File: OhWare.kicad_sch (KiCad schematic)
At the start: 1 part, among them J1 Screw_Terminal_01x03

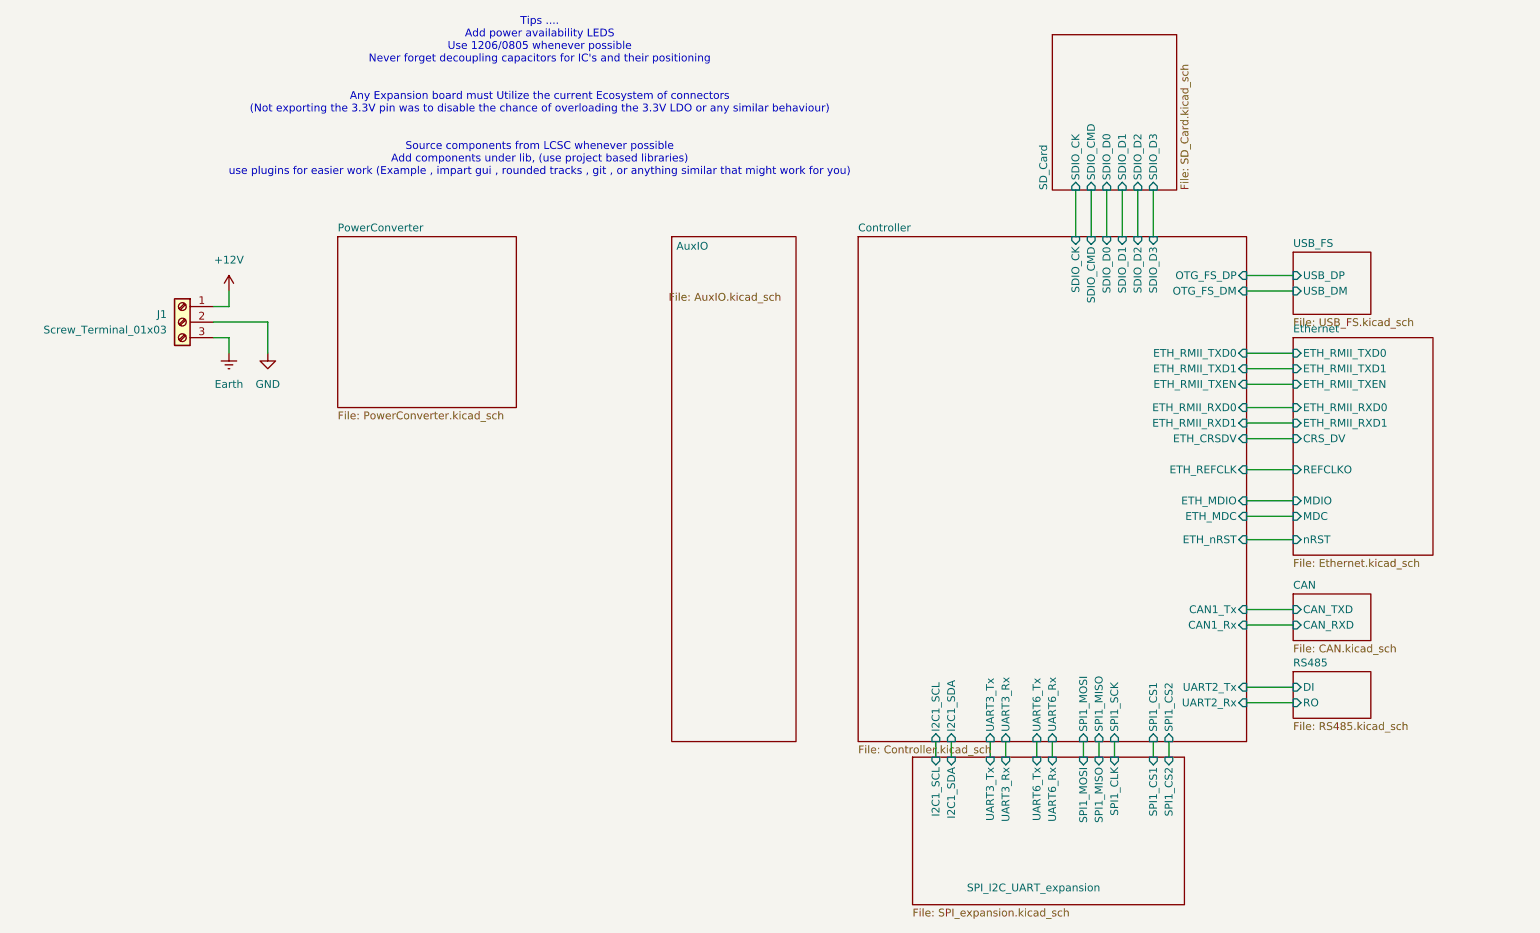
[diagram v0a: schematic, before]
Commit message: Done routing for Buck Converter , Rs485 and CAN , Some Routing for MCU and associated circuitry , NO ETHERNET ROUTING , NO module Interconnects yet
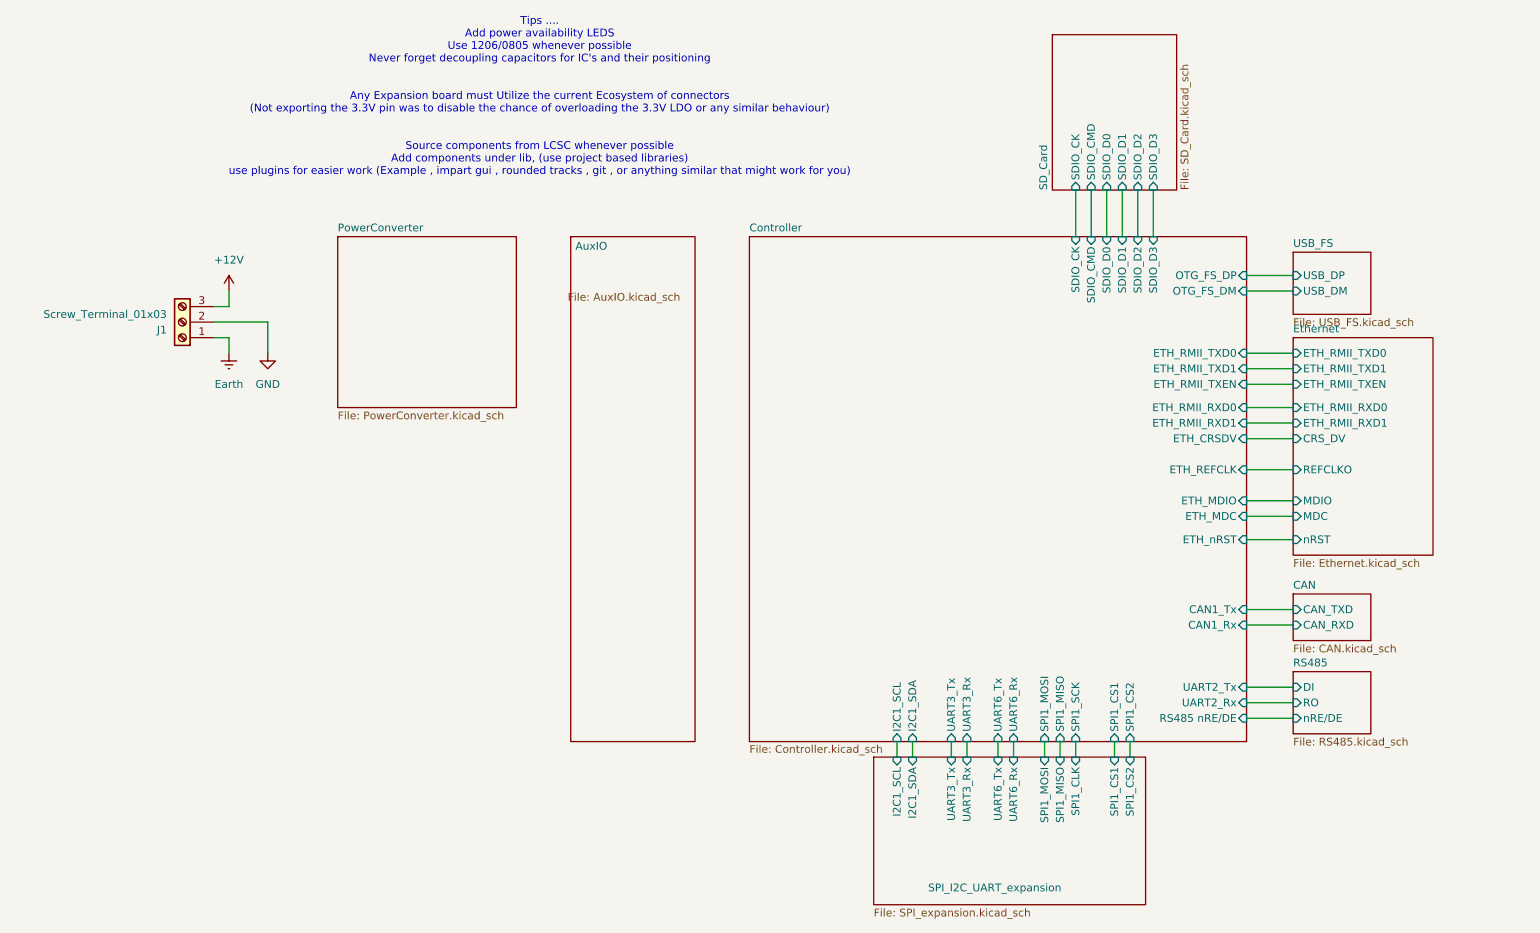
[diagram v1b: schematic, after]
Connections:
- net +12V: now also J1.3 (Pin_3); no longer J1.1 (Pin_1)
- net Earth: now also J1.1 (Pin_1); no longer J1.3 (Pin_3)
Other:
- sheet Controller ports: added RS485 nRE/DE; removed none
- sheet RS485 ports: added nRE/DE; removed none
- moved on the sheet: J1

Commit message: Added Base
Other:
- removed sheet Ethernet
- removed sheet SD_Card
- removed sheet USB_FS
- added sheet Esp32 (Esp32.kicad_sch)
- sheet Controller ports: added none; removed ETH_CRSDV, ETH_MDC, ETH_MDIO, ETH_REFCLK, ETH_RMII_RXD0, ETH_RMII_RXD1, ETH_RMII_TXD0, ETH_RMII_TXD1, ETH_RMII_TXEN, ETH_nRST, OTG_FS_DM, OTG_FS_DP, SDIO_CK, SDIO_CMD, SDIO_D0, SDIO_D1, SDIO_D2, SDIO_D3

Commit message: UPDATED
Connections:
- net +12V: now also J1.1 (Pin_1); no longer J1.3 (Pin_3)
- net Earth: now also J1.3 (Pin_3); no longer J1.1 (Pin_1)
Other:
- sheet Esp32 ports: added EN, SPI_CLK, SPI_CS, SPI_MISO, SPI_MOSI; removed none
- moved on the sheet: J1
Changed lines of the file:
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@@
 	(symbol
 		(lib_id "Connector:Screw_Terminal_01x03")
-		(at 40.64 69.85 180)
+		(at 40.64 69.85 0)
+		(mirror y)
 		(unit 1)
 		(exclude_from_sim no)
@@
 		(dnp no)
 		(property "Reference" "J1"
-			(at 38.1 71.1201 0)
+			(at 38.1 68.5799 0)
 			(effects
 				(font
@@
 		)
 		(property "Value" "Screw_Terminal_01x03"
-			(at 38.1 68.5801 0)
+			(at 38.1 71.1199 0)
 			(effects
 				(font
@@
 	)
 	(sheet
-		(at 222.25 72.39)
-		(size 19.05 21.59)
+		(at 222.25 73.66)
+		(size 19.05 17.78)
 		(exclude_from_sim no)
 		(in_bom yes)
@@
 		)
 		(property "Sheetname" "Esp32"
-			(at 222.25 71.6784 0)
+			(at 222.25 72.9484 0)
 			(effects
 				(font
@@
 		)
 		(property "Sheetfile" "Esp32.kicad_sch"
-			(at 222.25 94.5646 0)
+			(at 222.25 92.0246 0)
 			(effects
 				(font
@@
 			)
 		)
+		(pin "EN" input
+			(at 222.25 77.47 180)
+			(effects
+				(font
+					(size 1.27 1.27)
+				)
+				(justify left)
+			)
+		)
+		(pin "SPI_CLK" input
+			(at 222.25 80.01 180)
+			(effects
+				(font
+					(size 1.27 1.27)
+				)
+				(justify left)
+			)
+		)
+		(pin "SPI_CS" input
+			(at 222.25 82.55 180)
+			(effects
+				(font
+					(size 1.27 1.27)
+				)
+				(justify left)
+			)
+		)
+		(pin "SPI_MISO" input
+			(at 222.25 85.09 180)
+			(effects
+				(font
+					(size 1.27 1.27)
+				)
+				(justify left)
+			)
+		)
+		(pin "SPI_MOSI" input
+			(at 222.25 87.63 180)
+			(effects
+				(font
+					(size 1.27 1.27)
+				)
+				(justify left)
+			)
+		)

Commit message: Latest Changes
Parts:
- added JP1: Jumper_2_Bridged, Jumper:Jumper_Harwin_S1621_P10.9mm, symbol Jumper:Jumper_2_Bridged
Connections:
- net Esp32/SPI_MISO: now also JP1.2 (B)
- new net Controller/SPI3_MISO: JP1.1 (A)
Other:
- sheet Controller ports: added CAN1_RX, CAN1_TX, SPI3_DEN, SPI3_MISO, SPI3_MOSI, SPI3_SCK, USART3_RX, USART3_TX; removed CAN1_Rx, CAN1_Tx, UART2_Rx, UART2_Tx
- moved on the sheet: J1
